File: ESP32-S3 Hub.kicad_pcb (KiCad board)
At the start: 6 copper layers, 15 x 30 mm, 73 parts, among them J1 Precidip 853-87-004-20-001101, J10 Precidip 853-87-004-20-001101, J11 FPC 0.3mm Aces 51688-0070M, J12 Precidip 853-87-004-20-001101, J13 TE 3-2363961-0 receptacle, J15 Precidip 853-87-004-20-001101, J16 TE 3-2363961-0 receptacle, J18 Precidip 852-10-004-20-001101, J2 Precidip 853-87-004-20-001101, J3 FPC 0.3mm Aces 51688-0070M, J4 Precidip 853-87-004-20-001101, J5 FPC 0.3mm Aces 51688-0070M, J6 Precidip 853-87-004-20-001101, J7 Precidip 853-87-004-20-001101, J8 FPC 0.3mm Aces 51688-0070M, J9 Precidip 853-87-004-20-001101, SW1 Mitsumi R-667996, SW2 Mitsumi R-667996, U1 ESP32-S3 FN8, U2 SN74LV595A, U3 THVD1420DRLR, U4 TPS2521ARPWR, U5 SN74LV595A, U6 TS5A3159DCK, Y1 2 pin 40MHZ, 10ppm tol., 20pp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

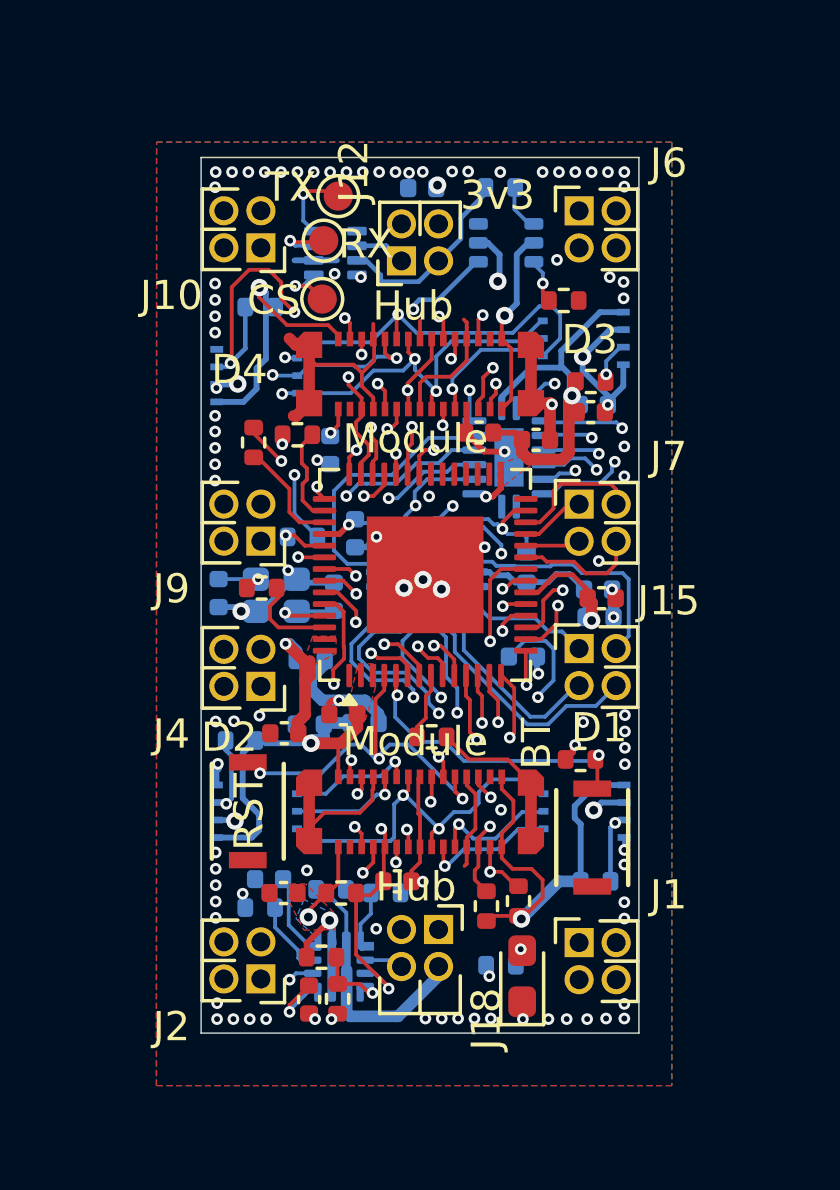
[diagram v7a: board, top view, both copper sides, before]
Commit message: Updated Silkscreen, version info
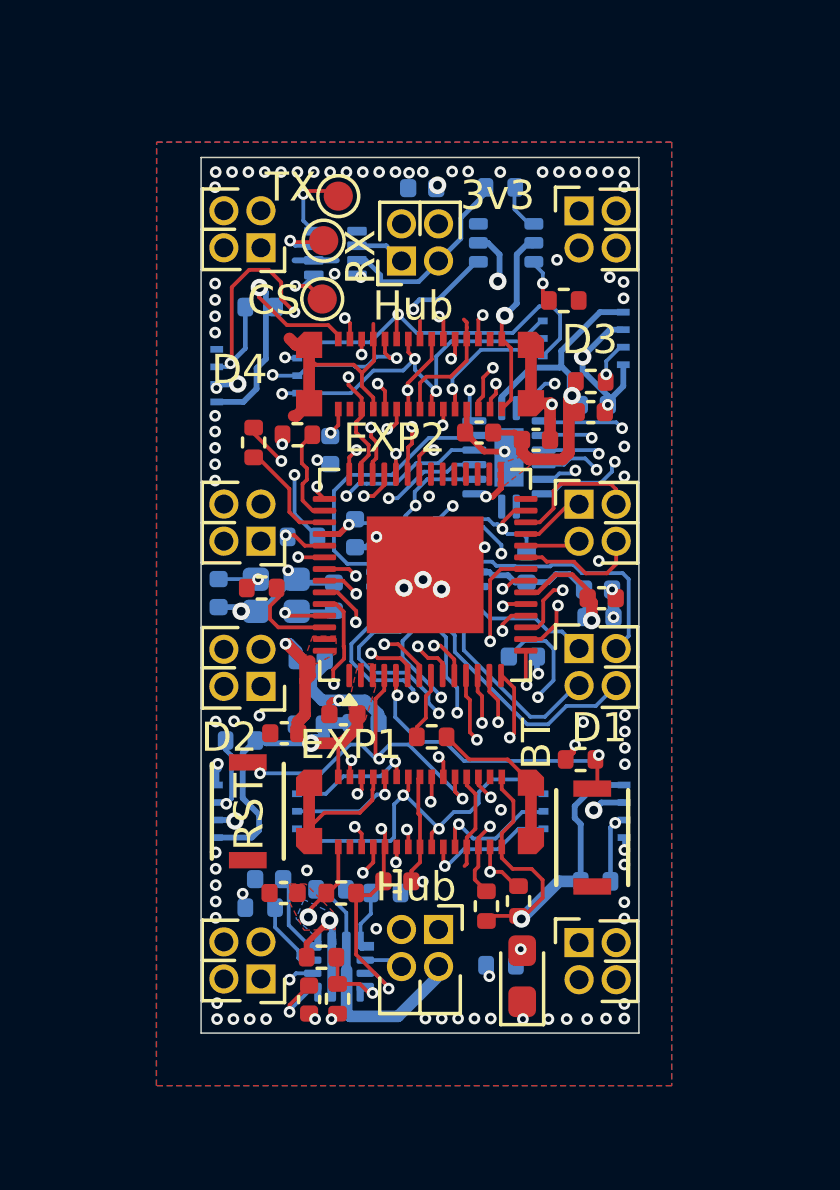
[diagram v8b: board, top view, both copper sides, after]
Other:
- board text added: "Asher E ${REVISION}"
- board text added: "EXP1"
- board text added: "EXP2"
- board text added: "SPI1"
- board text added: "SPI2"
- board text added: "SPI3"
- board text added: "SPI4"
- board text removed: "Module"
- board text removed: "SPI"
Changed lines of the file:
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@@
 	(title_block
 		(title "CACKLE - Hub")
-		(date "2024-10-20")
-		(rev "V1")
+		(date "2025-11-14")
+		(rev "V2")
 		(comment 1 "Licensed under CERN-OHL-S v2")
 		(comment 2 "Author: Asher Edwards")
@@
 			(at 3.0675 -1.635 0)
 			(layer "F.SilkS")
+			(hide yes)
 			(effects
 				(font
@@
 			(at 3.0675 -1.635 0)
 			(layer "F.SilkS")
+			(hide yes)
 			(effects
 				(font
@@
 			(at 3.0675 -1.635 90)
 			(layer "F.SilkS")
+			(hide yes)
 			(effects
 				(font
@@
 			(at 3.0675 -1.635 180)
 			(layer "F.SilkS")
+			(hide yes)
 			(effects
 				(font
@@
 			(at 3.0675 -1.635 180)
 			(layer "F.SilkS")
+			(hide yes)
 			(effects
 				(font
@@
 			(at 3.0675 -1.635 180)
 			(layer "F.SilkS")
+			(hide yes)
 			(effects
 				(font
@@
 			(at 3.0675 -1.635 180)
 			(layer "F.SilkS")
+			(hide yes)
 			(effects
 				(font
@@
 			(at 3.0675 -1.635 270)
 			(layer "F.SilkS")
+			(hide yes)
 			(effects
 				(font
@@
 			(at 3.0675 -1.635 0)
 			(layer "F.SilkS")
+			(hide yes)
 			(effects
 				(font
@@
 			(at 3.0675 -1.635 0)
 			(layer "F.SilkS")
+			(hide yes)
 			(effects
 				(font
@@
 	)
 	(gr_text "RX"
-		(at 152.6 85.35 0)
+		(at 153.955 86.155 90)
 		(layer "F.SilkS")
 		(effects
@@
 		)
 	)
-	(gr_text "Module"
-		(at 152.75 102.4 0)
+	(gr_text "EXP1"
+		(at 151.275 102.5 0)
 		(layer "F.SilkS" knockout)
 		(effects
@@
 		)
 	)
-	(gr_text "Module"
-		(at 152.75 92.025 0)
+	(gr_text "EXP2"
+		(at 152.775 92 0)
 		(layer "F.SilkS" knockout)
 		(effects
@@
 		)
 	)
-	(gr_text "SPI"
-		(at 158.9 86.525 90)
-		(layer "B.SilkS")
+	(gr_text "SPI3"
+		(at 158.325 86.2 90)
+		(layer "B.SilkS" knockout)
 		(effects
 			(font
@@
 		)
 	)
-	(gr_text "SPI"
-		(at 151.775 90.225 270)
-		(layer "B.SilkS")
+	(gr_text "SPI4"
+		(at 151.8 90.65 270)
+		(layer "B.SilkS" knockout)
 		(effects
 			(font
@@
 		)
 	)
-	(gr_text "SPI"
-		(at 152.1 105.2 270)
-		(layer "B.SilkS")
+	(gr_text "SPI2"
+		(at 151.975 106 270)
+		(layer "B.SilkS" knockout)
 		(effects
 			(font
@@
 		)
 	)
-	(gr_text "SPI"
-		(at 159.2 102.75 90)
-		(layer "B.SilkS")
+	(gr_text "SPI1"
+		(at 159.025 102.425 90)
+		(layer "B.SilkS" knockout)
 		(effects
 			(font
@@
 			)
 			(justify left bottom mirror)
+		)
+	)
+	(gr_text "Asher E ${REVISION}"
+		(at 162.5 101.85 0)
+		(layer "B.SilkS")
+		(effects
+			(font
+				(size 1 1)
+				(thickness 0.125)
+			)
+			(justify left bottom mirror)
